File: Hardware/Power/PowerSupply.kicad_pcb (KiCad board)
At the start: 4 copper layers, 172 x 85 mm, 206 parts, among them Q1 PSMN1R5-25MLHX, Q10 BSS84, Q11 2N7002PW, Q12 2N7002PW, Q13 2N7002PW, Q14 Si7141DP, Q15 BSS84, Q16 Si7141DP, Q17 Si7141DP, Q18 Si7141DP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

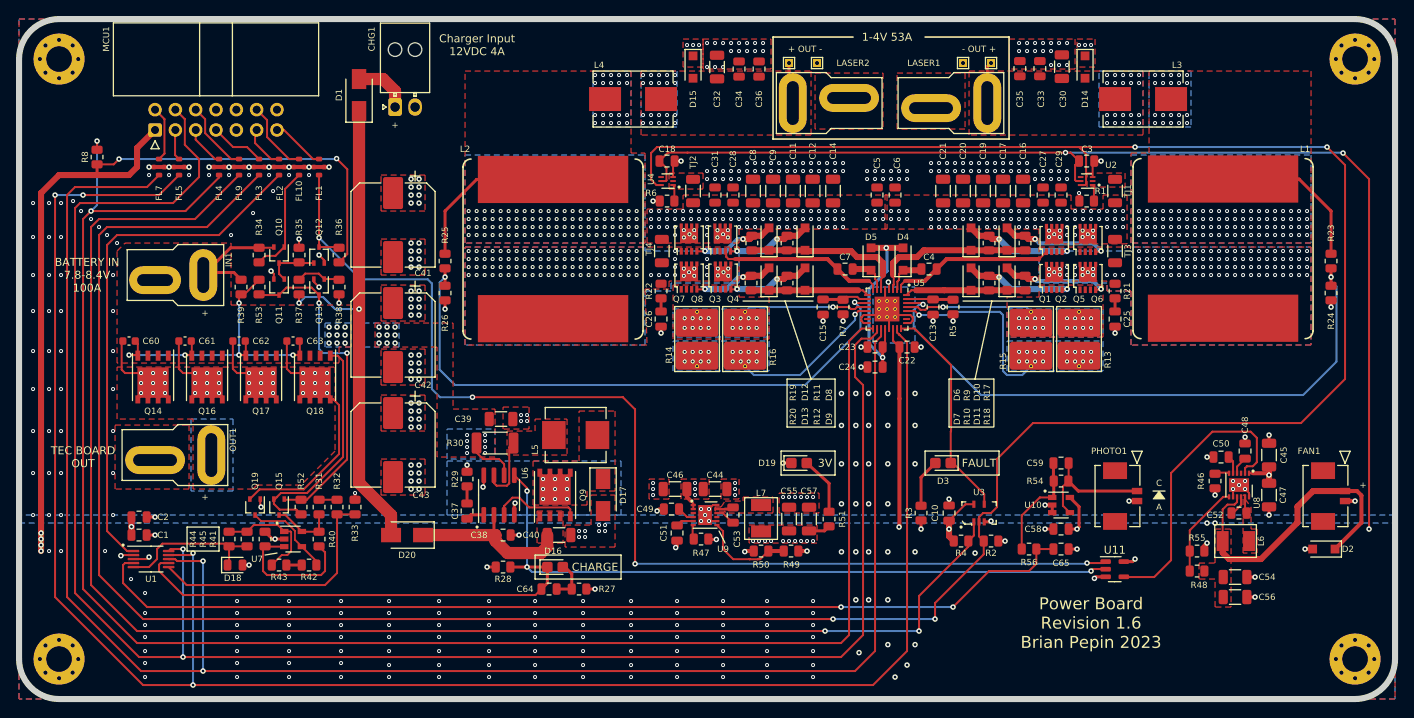
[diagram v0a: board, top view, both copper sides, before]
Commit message: Update to kicad 8
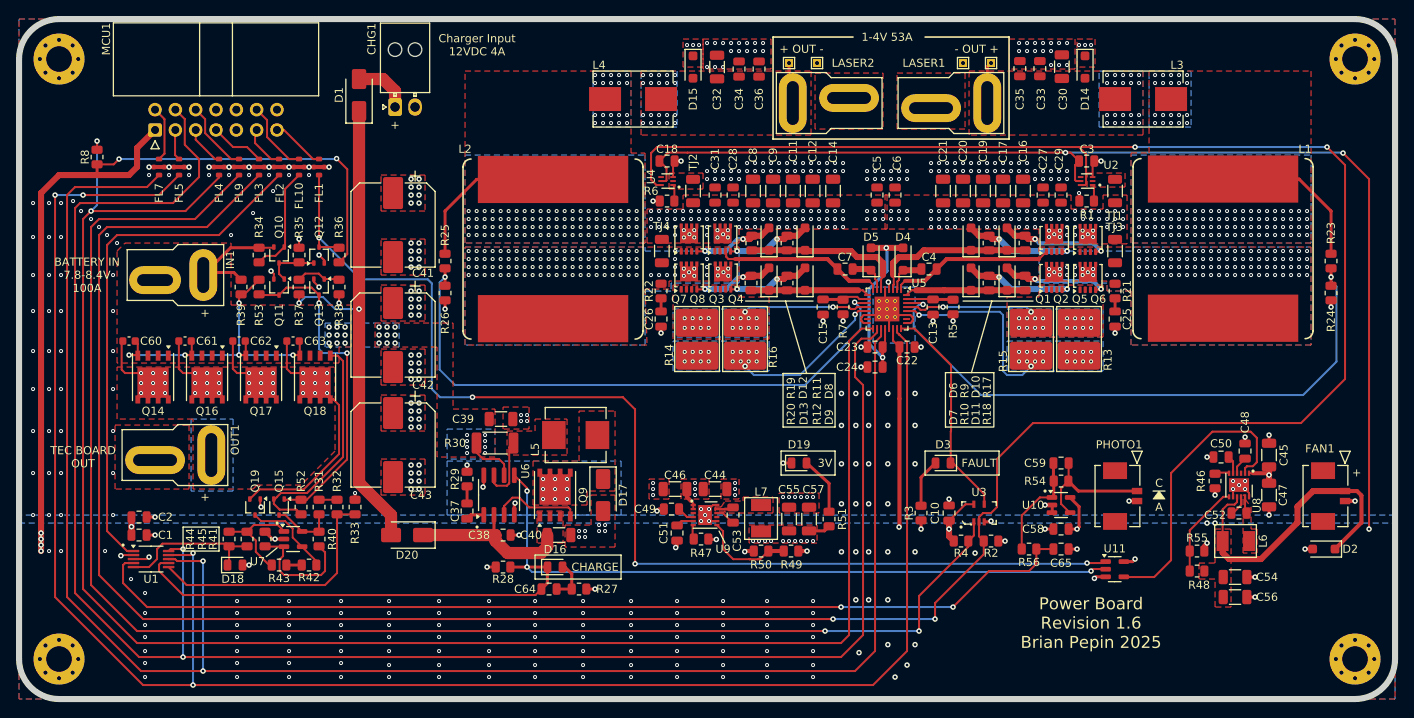
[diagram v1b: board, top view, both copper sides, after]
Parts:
- D16, D19, D3: footprint LED_SMD:LED_0805_2012Metric_Castellated -> LED_SMD:LED_0805_2012Metric
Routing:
- net Net-(U7-+): track 17.2 -> 15.5 mm
- net Net-(R43-Pad2): track 14.0 -> 13.2 mm
- net Net-(U5-CSP2): vias 17 -> 18
- net Net-(U5-CSP1): vias 17 -> 18
- net GND: vias 457 -> 459
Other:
- board text added: "Power Board Revision 1.6 Brian Pepin 2025"
- board text removed: "Power Board Revision 1.6 Brian Pepin 2023"
